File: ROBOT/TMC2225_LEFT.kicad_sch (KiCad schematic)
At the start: 16 parts, among them J3 Conn_01x04, U2 TMC2225-SA-T

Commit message: Schema OK
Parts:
- C1, C2: footprint Capacitor_SMD:C_0603_1608Metric_Pad1.08x0.95mm_HandSolder -> Capacitor_SMD:C_0805_2012Metric_Pad1.18x1.45mm_HandSolder
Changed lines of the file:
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@@
 			)
 		)
-		(property "Footprint" "Capacitor_SMD:C_0603_1608Metric_Pad1.08x0.95mm_HandSolder"
+		(property "Footprint" "Capacitor_SMD:C_0805_2012Metric_Pad1.18x1.45mm_HandSolder"
 			(at 161.29 51.1048 0)
 			(effects
@@
 			)
 		)
-		(property "Footprint" "Capacitor_SMD:C_0603_1608Metric_Pad1.08x0.95mm_HandSolder"
+		(property "Footprint" "Capacitor_SMD:C_0805_2012Metric_Pad1.18x1.45mm_HandSolder"
 			(at 161.29 59.9948 0)
 			(effects

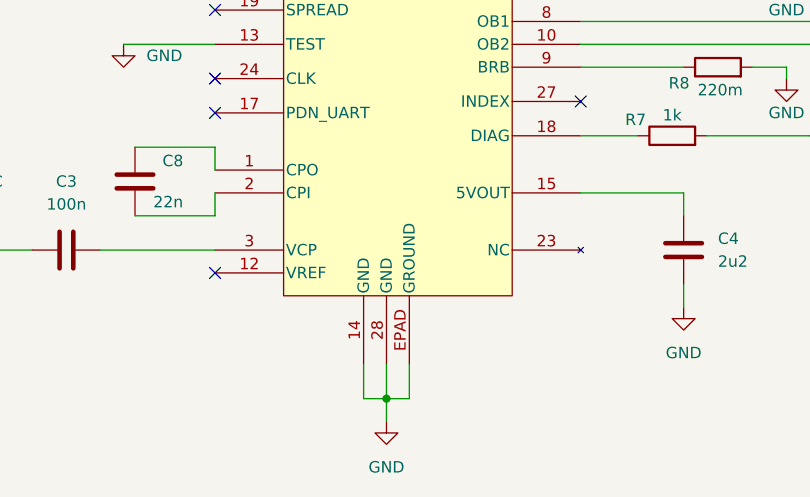
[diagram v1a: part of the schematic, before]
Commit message: GND PAD 29 TMC22225
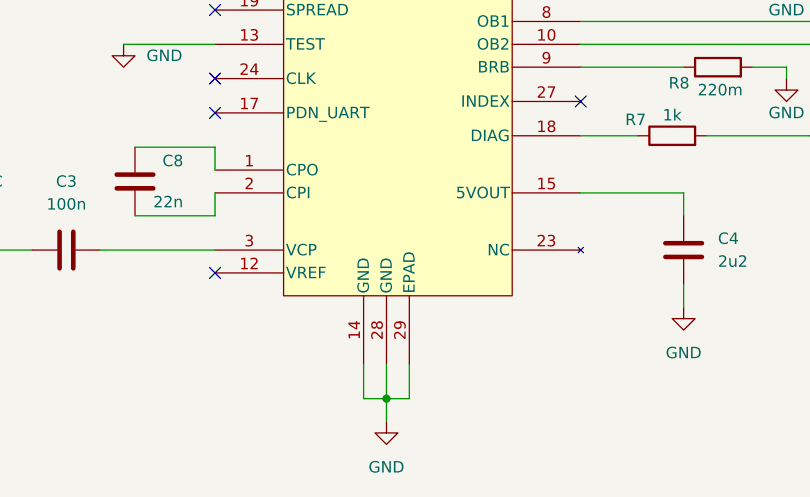
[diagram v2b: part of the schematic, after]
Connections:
- net GND: now also U2.29 (EPAD); no longer U2.EPAD (GROUND)
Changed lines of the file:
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@@
 			)
 		)
-		(property "Datasheet" "TMC2225-SA"
+		(property "Datasheet" "TMC2225-SA-T"
 			(at 184.15 99.06 0)
 			(effects
@@
 		(pin "2"
 		)
-		(pin "EPAD"
+		(pin "29"
 		)
 		(pin "14"

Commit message: add condo
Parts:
- added C9: 10uF, Capacitor_SMD:C_0805_2012Metric_Pad1.18x1.45mm_HandSolder, symbol Device:C
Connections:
- net GND: now also C9.2
- net VCC: now also C9.1
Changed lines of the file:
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@@
+	)
+	(junction
+		(at 149.86 41.91)
+		(diameter 0)
+		(color 0 0 0 0)
 	)
 	(junction
@@
 	(wire
 		(pts
+			(xy 163.83 41.91) (xy 163.83 44.45)
+		)
+		(stroke
+			(width 0)
+			(type default)
+		)
+	)
+	(wire
+		(pts
 			(xy 133.35 58.42) (xy 140.97 58.42)
 		)
@@
 	(wire
 		(pts
-			(xy 149.86 38.1) (xy 149.86 52.07)
+			(xy 149.86 38.1) (xy 149.86 41.91)
 		)
 		(stroke
@@
 	(wire
 		(pts
+			(xy 149.86 41.91) (xy 149.86 52.07)
+		)
+		(stroke
+			(width 0)
+			(type default)
+		)
+	)
+	(wire
+		(pts
 			(xy 199.39 91.44) (xy 208.28 91.44)
 		)
@@
 	(wire
 		(pts
+			(xy 161.29 41.91) (xy 163.83 41.91)
+		)
+		(stroke
+			(width 0)
+			(type default)
+		)
+	)
+	(wire
+		(pts
 			(xy 90.17 104.14) (xy 90.17 105.41)
 		)
@@
 		(pts
 			(xy 161.29 52.07) (xy 163.83 52.07)
+		)
+		(stroke
+			(width 0)
+			(type default)
+		)
+	)
+	(wire
+		(pts
+			(xy 149.86 41.91) (xy 153.67 41.91)
 		)
 		(stroke
@@
 	)
 	(symbol
+		(lib_id "power:GND")
+		(at 163.83 44.45 0)
+		(unit 1)
+		(exclude_from_sim no)
+		(in_bom yes)
+		(on_board yes)
+		(dnp no)
+		(fields_autoplaced yes)
+		(property "Reference" "#PWR034"
+			(at 163.83 50.8 0)
+			(effects
+				(font
+					(size 1.27 1.27)
+				)
+				(hide yes)
+			)
+		)
+		(property "Value" "GND"
+			(at 163.83 49.53 0)
+			(effects
+				(font
+					(size 1.27 1.27)
+				)
+			)
+		)
+		(property "Footprint" ""
+			(at 163.83 44.45 0)
+			(effects
+				(font
+					(size 1.27 1.27)
+				)
+				(hide yes)
+			)
+		)
+		(property "Datasheet" ""
+			(at 163.83 44.45 0)
+			(effects
+				(font
+					(size 1.27 1.27)
+				)
+				(hide yes)
+			)
+		)
+		(property "Description" "Power symbol creates a global label with name \"GND\" , ground"
+			(at 163.83 44.45 0)
+			(effects
+				(font
+					(size 1.27 1.27)
+				)
+				(hide yes)
+			)
+		)
+		(pin "1"
+		)
+		(instances
+			(project "Robot"
+				(path "/f1dd5862-79ad-43be-9f5c-46baed2cd441/7dc21443-1a57-41ca-89e9-e7c3f2f9d506"
+					(reference "#PWR034")
+					(unit 1)
+				)
+			)
+		)
+	)
+	(symbol
 		(lib_id "power:+3.3V")
 		(at 140.97 57.15 0)
@@
 					(unit 1)
 				)
+			)
+		)
+	)
+	(symbol
+		(lib_id "Device:C")
+		(at 157.48 41.91 90)
+		(unit 1)
+		(exclude_from_sim no)
+		(in_bom yes)
+		(on_board yes)
+		(dnp no)
+		(property "Reference" "C9"
+			(at 157.734 36.322 90)
+			(effects
+				(font
+					(size 1.27 1.27)
+				)
+			)
+		)
+		(property "Value" "10uF"
+			(at 157.48 38.608 90)
+			(effects
+				(font
+					(size 1.27 1.27)
+				)
+			)
+		)
+		(property "Footprint" "Capacitor_SMD:C_0805_2012Metric_Pad1.18x1.45mm_HandSolder"
+			(at 161.29 40.9448 0)
+			(effects
+				(font
+					(size 1.27 1.27)
+				)
+				(hide yes)
+			)
+		)
+		(property "Datasheet" "~"
+			(at 157.48 41.91 0)
+			(effects
+				(font
+					(size 1.27 1.27)
+				)
+				(hide yes)
+			)
+		)
+		(property "Description" "Unpolarized capacitor"
+			(at 157.48 41.91 0)
+			(effects
+				(font
+					(size 1.27 1.27)
+				)
+				(hide yes)
+			)
+		)
+		(pin "1"
+		)
+		(pin "2"
+		)
+		(instances
+			(project "Robot"
+				(path "/f1dd5862-79ad-43be-9f5c-46baed2cd441/7dc21443-1a57-41ca-89e9-e7c3f2f9d506"
+					(reference "C9")
+					(unit 1)
+				)

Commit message: stach
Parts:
- C1, C2: footprint Capacitor_SMD:C_0805_2012Metric_Pad1.18x1.45mm_HandSolder -> Capacitor_SMD:C_0603_1608Metric_Pad1.08x0.95mm_HandSolder
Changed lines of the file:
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@@
 			)
 		)
-		(property "Footprint" "Capacitor_SMD:C_0805_2012Metric_Pad1.18x1.45mm_HandSolder"
+		(property "Footprint" "Capacitor_SMD:C_0603_1608Metric_Pad1.08x0.95mm_HandSolder"
 			(at 161.29 51.1048 0)
 			(effects
@@
 			)
 		)
-		(property "Footprint" "Capacitor_SMD:C_0805_2012Metric_Pad1.18x1.45mm_HandSolder"
+		(property "Footprint" "Capacitor_SMD:C_0603_1608Metric_Pad1.08x0.95mm_HandSolder"
 			(at 161.29 59.9948 0)
 			(effects
